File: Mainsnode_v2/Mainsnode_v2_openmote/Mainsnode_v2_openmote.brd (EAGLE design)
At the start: 72.6 x 47.1 mm, 72 parts, among them IC1 7805T, J2 WIRE_HOLE-14AWG, J3 WIRE_HOLE-14AWG, J4 HOLE, J5 HOLE, J6 HOLE, J7 HOLE, K1 S216S01F, Q1 STGD5NB120SZT4, Q2 3.579545MHz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

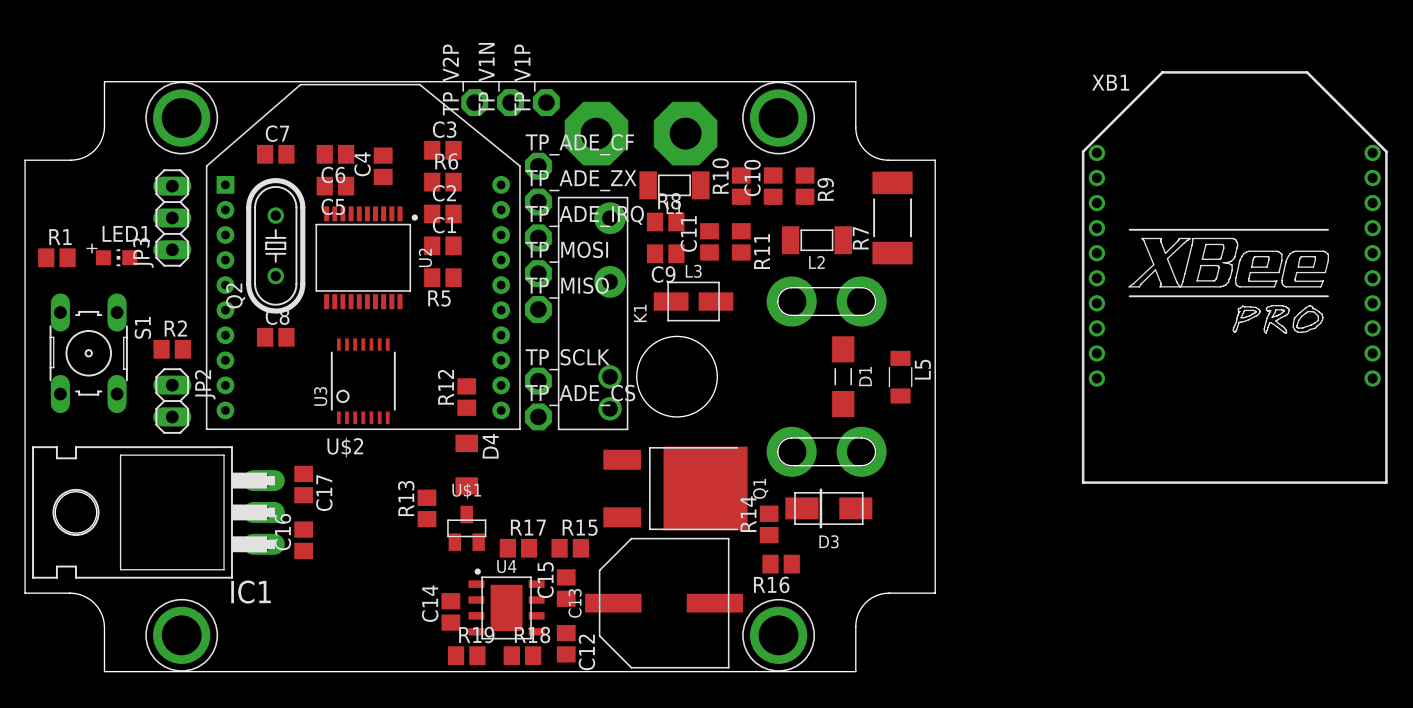
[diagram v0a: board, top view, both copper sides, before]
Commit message: Finish PCB Mainsnode_V2_openmote
Ferrite bead DigiKey 240-2418 and 240-2520 and casing have not been
ordered yet.
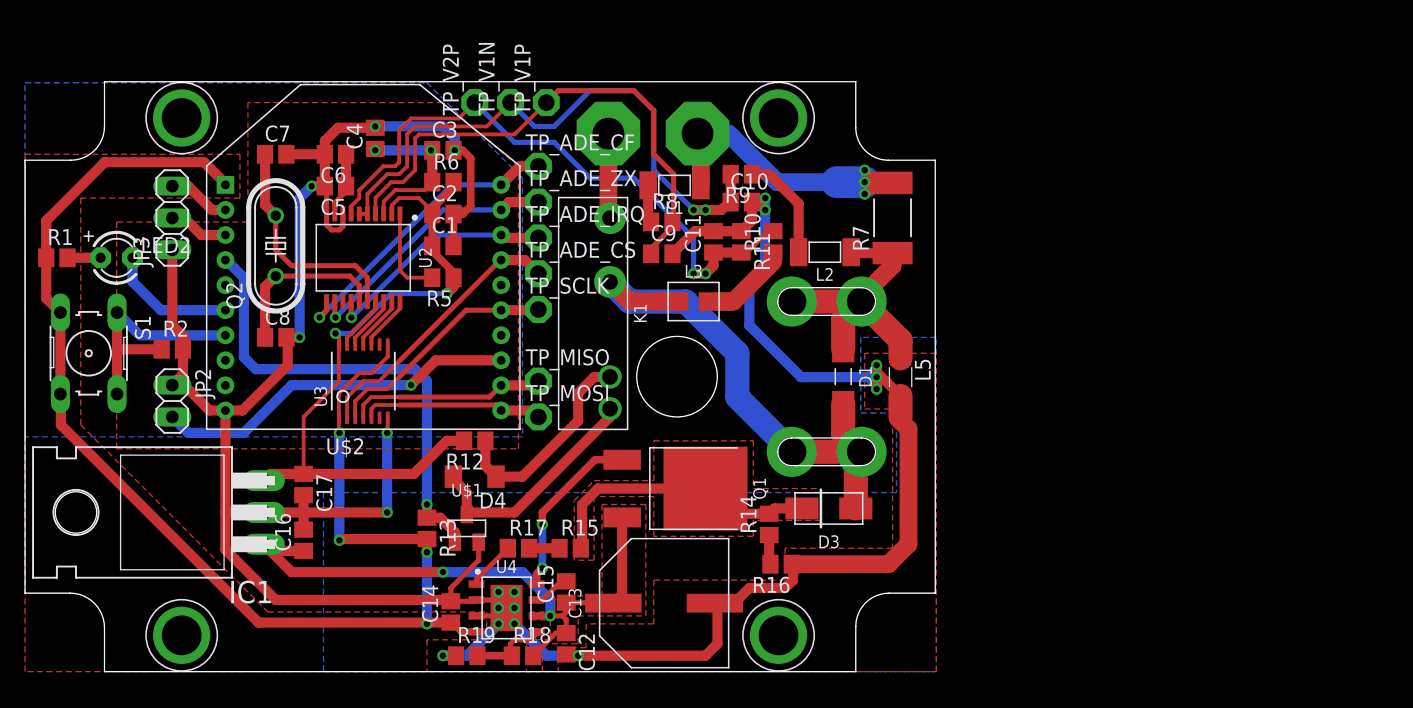
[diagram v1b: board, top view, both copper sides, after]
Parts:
- removed LED1: (no value), adafruit:CHIP-LED0805
- removed XB1: XBEE-PRO, maxstream:XBEE-PRO
- added LED2: (no value), adafruit:LED3MM
- moved TP_ADE_CS 11.4 mm to (41.0, 31.8)
- moved TP_MOSI 11.4 mm to (41.0, 20.3)
- moved TP_MISO 5.71 mm to (41.0, 23.2)
- moved TP_SCLK 5.71 mm to (41.0, 28.9)
- moved R9 5.17 mm to (57.1, 39.7), turned to 180 degrees
- moved R10 5.12 mm to (59.7, 34.3)
- moved R12 3.55 mm to (35.9, 18.4), turned to 180 degrees
- moved C10 2.84 mm to (57.1, 37.5), turned to 0 degrees
- moved C4 2.31 mm to (27.9, 42.5)
- moved R13 1.59 mm to (32.1, 11.4), turned to 270 degrees
- moved L2 1.14 mm to (63.8, 33.5)
- moved D4 1.14 mm to (35.9, 15.6), turned to 180 degrees
- moved J3 0.95 mm to (53.7, 42.9)
- moved J2 0.95 mm to (46.5, 42.9)
- moved C11 0.32 mm to (54.9, 34.3)
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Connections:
- removed net GND_NC: XB1.10
- removed net VCC_NC: XB1.1
- net ADE_CS: now also U$2.17; no longer U$2.11
- net MISO: now also U$2.12; no longer U$2.15
- net MOSI: now also U$2.11; no longer U$2.17
- net N$2: now also LED2.A; no longer LED1.A
- net RELAY_LED: now also LED2.K; no longer LED1.C
- net SCLK: now also U$2.15; no longer U$2.12
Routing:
- net GND: track 0.00 -> 246.6 mm, vias 0 -> 19
- net 3V3: track 0.00 -> 105.5 mm, vias 0 -> 4
- net 5V: track 0.00 -> 55.1 mm, vias 0 -> 2
- net V2P: track 0.00 -> 49.9 mm, vias 0 -> 2
- net VDC: track 0.00 -> 48.7 mm, vias 0 -> 2
- net V1N: track 0.00 -> 47.9 mm, vias 0 -> 2
- net WALL_PHASE: track 0.00 -> 42.4 mm
- net V1P: track 0.00 -> 42.2 mm
- net RELAY_CTRL: track 0.00 -> 38.2 mm, vias 0 -> 1
- net PROG_CTRL: track 0.00 -> 29.2 mm, vias 0 -> 1
- net WALL_NEUTRAL: track 0.00 -> 24.0 mm
- net LOAD_NEUTRAL: track 0.00 -> 24.0 mm, vias 0 -> 3
- net ADE_CF: track 0.00 -> 24.0 mm, vias 0 -> 1
- net N$13: track 0.00 -> 22.6 mm
- net ADE_CS: track 0.00 -> 21.9 mm
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- added copper zone on layer 1, net 3V3
- added copper zone on layer 1, net GND
- added copper zone on layer 16, net GND
- added copper zone on layer 1, net N$13
- added copper zone on layer 1, net VDC
